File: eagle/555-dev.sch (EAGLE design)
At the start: 28 parts, among them IC1 NE555, Q1 IRF740, T1 2N2222

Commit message: change CAP
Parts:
- C2, C3, C4: device SparkFun-Passives:CAPPTH -> SparkFun-Passives:CAPPTH1
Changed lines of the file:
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@@
 <part name="R4" library="SparkFun-Resistors" deviceset="RESISTOR" device="PTH-1/4W" value="220"/>
 <part name="GND1" library="supply1" deviceset="GND" device=""/>
-<part name="C2" library="SparkFun-Passives" deviceset="CAP" device="PTH" value="0.01uF"/>
+<part name="C2" library="SparkFun-Passives" deviceset="CAP" device="PTH1" value="0.01uF"/>
 <part name="GND2" library="supply1" deviceset="GND" device=""/>
 <part name="T1" library="adafruit" deviceset="2N2222" device=""/>
@@
 <part name="GND7" library="supply1" deviceset="GND" device=""/>
 <part name="R1" library="SparkFun-Resistors" deviceset="RESISTOR" device="PTH-1/4W" value="1K"/>
-<part name="C4" library="SparkFun-Passives" deviceset="CAP" device="PTH" value="0.1uF"/>
+<part name="C4" library="SparkFun-Passives" deviceset="CAP" device="PTH1" value="0.1uF"/>
 <part name="VR" library="SparkFun-Electromechanical" deviceset="POT" device="ALPS-KIT" value="50K"/>
 <part name="GND9" library="supply1" deviceset="GND" device=""/>
@@
 <part name="P+6" library="supply1" deviceset="VCC" device=""/>
 <part name="GND8" library="supply1" deviceset="GND" device=""/>
-<part name="C3" library="SparkFun-Passives" deviceset="CAP" device="PTH" value="0.1uF"/>
+<part name="C3" library="SparkFun-Passives" deviceset="CAP" device="PTH1" value="0.1uF"/>
 <part name="GND10" library="supply1" deviceset="GND" device=""/>
 <part name="P+1" library="supply1" deviceset="VCC" device=""/>

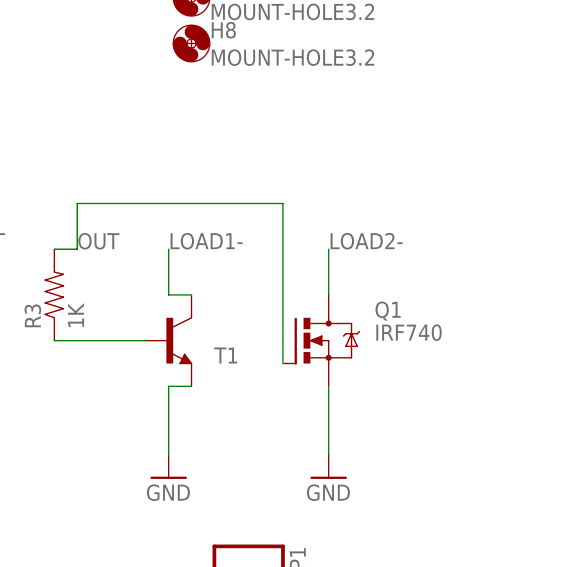
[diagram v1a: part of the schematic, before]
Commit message: add R2 base resistor and change Q1 into TIP120/IRF740
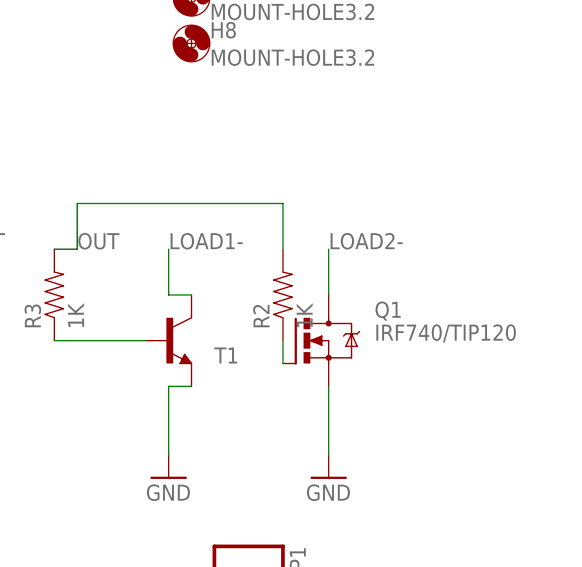
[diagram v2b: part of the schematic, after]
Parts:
- added R2: 1K, SparkFun-Resistors:RESISTORPTH-1/4W
- Q1: value IRF740 -> IRF740/TIP120
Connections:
- new net N$1: Q1.G, R2.1
- net OUT: now also R2.2; no longer Q1.G
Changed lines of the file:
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@@
 <?xml version="1.0" encoding="utf-8"?>
 <!DOCTYPE eagle SYSTEM "eagle.dtd">
-<eagle version="7.4.0">
+<eagle version="7.2.0">
 <drawing>
 <settings>
@@
 <grid distance="0.1" unitdist="inch" unit="inch" style="lines" multiple="1" display="no" altdistance="0.01" altunitdist="inch" altunit="inch"/>
 <layers>
-<layer number="1" name="Top" color="4" fill="1" visible="yes" active="no"/>
-<layer number="16" name="Bottom" color="1" fill="1" visible="yes" active="no"/>
-<layer number="17" name="Pads" color="2" fill="1" visible="yes" active="no"/>
-<layer number="18" name="Vias" color="2" fill="1" visible="yes" active="no"/>
-<layer number="19" name="Unrouted" color="6" fill="1" visible="yes" active="no"/>
-<layer number="20" name="Dimension" color="15" fill="1" visible="yes" active="no"/>
-<layer number="21" name="tPlace" color="7" fill="1" visible="yes" active="no"/>
-<layer number="22" name="bPlace" color="7" fill="1" visible="yes" active="no"/>
-<layer number="23" name="tOrigins" color="15" fill="1" visible="yes" active="no"/>
-<layer number="24" name="bOrigins" color="15" fill="1" visible="yes" active="no"/>
-<layer number="25" name="tNames" color="7" fill="1" visible="yes" active="no"/>
-<layer number="26" name="bNames" color="7" fill="1" visible="yes" active="no"/>
-<layer number="27" name="tValues" color="7" fill="1" visible="yes" active="no"/>
-<layer number="28" name="bValues" color="7" fill="1" visible="yes" active="no"/>
+<layer number="1" name="Top" color="4" fill="1" visible="no" active="no"/>
+<layer number="16" name="Bottom" color="1" fill="1" visible="no" active="no"/>
+<layer number="17" name="Pads" color="2" fill="1" visible="no" active="no"/>
+<layer number="18" name="Vias" color="2" fill="1" visible="no" active="no"/>
+<layer number="19" name="Unrouted" color="6" fill="1" visible="no" active="no"/>
+<layer number="20" name="Dimension" color="15" fill="1" visible="no" active="no"/>
+<layer number="21" name="tPlace" color="7" fill="1" visible="no" active="no"/>
+<layer number="22" name="bPlace" color="7" fill="1" visible="no" active="no"/>
+<layer number="23" name="tOrigins" color="15" fill="1" visible="no" active="no"/>
+<layer number="24" name="bOrigins" color="15" fill="1" visible="no" active="no"/>
+<layer number="25" name="tNames" color="7" fill="1" visible="no" active="no"/>
+<layer number="26" name="bNames" color="7" fill="1" visible="no" active="no"/>
+<layer number="27" name="tValues" color="7" fill="1" visible="no" active="no"/>
+<layer number="28" name="bValues" color="7" fill="1" visible="no" active="no"/>
 <layer number="29" name="tStop" color="7" fill="3" visible="no" active="no"/>
 <layer number="30" name="bStop" color="7" fill="6" visible="no" active="no"/>
@@
 <layer number="35" name="tGlue" color="7" fill="4" visible="no" active="no"/>
 <layer number="36" name="bGlue" color="7" fill="5" visible="no" active="no"/>
-<layer number="37" name="tTest" color="7" fill="1" visible="yes" active="no"/>
-<layer number="38" name="bTest" color="7" fill="1" visible="yes" active="no"/>
+<layer number="37" name="tTest" color="7" fill="1" visible="no" active="no"/>
+<layer number="38" name="bTest" color="7" fill="1" visible="no" active="no"/>
 <layer number="39" name="tKeepout" color="4" fill="11" visible="no" active="no"/>
 <layer number="40" name="bKeepout" color="1" fill="11" visible="no" active="no"/>
@@
 <layer number="44" name="Drills" color="7" fill="1" visible="no" active="no"/>
 <layer number="45" name="Holes" color="7" fill="1" visible="no" active="no"/>
-<layer number="46" name="Milling" color="3" fill="1" visible="yes" active="no"/>
-<layer number="47" name="Measures" color="7" fill="1" visible="yes" active="no"/>
-<layer number="48" name="Document" color="7" fill="1" visible="yes" active="no"/>
-<layer number="49" name="Reference" color="7" fill="1" visible="yes" active="no"/>
-<layer number="50" name="dxf" color="7" fill="1" visible="yes" active="no"/>
-<layer number="51" name="tDocu" color="7" fill="1" visible="yes" active="no"/>
-<layer number="52" name="bDocu" color="7" fill="1" visible="yes" active="no"/>
-<layer number="53" name="tGND_GNDA" color="7" fill="9" visible="yes" active="no"/>
-<layer number="54" name="bGND_GNDA" color="1" fill="9" visible="yes" active="no"/>
-<layer number="56" name="wert" color="7" fill="1" visible="yes" active="no"/>
-<layer number="57" name="tCAD" color="7" fill="1" visible="yes" active="no"/>
-<layer number="59" name="tCarbon" color="7" fill="1" visible="yes" active="no"/>
-<layer number="60" name="bCarbon" color="7" fill="1" visible="yes" active="no"/>
+<layer number="46" name="Milling" color="3" fill="1" visible="no" active="no"/>
+<layer number="47" name="Measures" color="7" fill="1" visible="no" active="no"/>
+<layer number="48" name="Document" color="7" fill="1" visible="no" active="no"/>
+<layer number="49" name="Reference" color="7" fill="1" visible="no" active="no"/>
+<layer number="50" name="dxf" color="7" fill="1" visible="no" active="no"/>
+<layer number="51" name="tDocu" color="7" fill="1" visible="no" active="no"/>
+<layer number="52" name="bDocu" color="7" fill="1" visible="no" active="no"/>
+<layer number="53" name="tGND_GNDA" color="7" fill="9" visible="no" active="no"/>
+<layer number="54" name="bGND_GNDA" color="1" fill="9" visible="no" active="no"/>
+<layer number="56" name="wert" color="7" fill="1" visible="no" active="no"/>
+<layer number="57" name="tCAD" color="7" fill="1" visible="no" active="no"/>
+<layer number="59" name="tCarbon" color="7" fill="1" visible="no" active="no"/>
+<layer number="60" name="bCarbon" color="7" fill="1" visible="no" active="no"/>
 <layer number="90" name="Modules" color="5" fill="1" visible="yes" active="yes"/>
 <layer number="91" name="Nets" color="2" fill="1" visible="yes" active="yes"/>
@@
 <part name="GND2" library="supply1" deviceset="GND" device=""/>
 <part name="T1" library="adafruit" deviceset="2N2222" device=""/>
-<part name="Q1" library="transistor-power" deviceset="IRF740" device=""/>
+<part name="Q1" library="transistor-power" deviceset="IRF740" device="" value="IRF740/TIP120"/>
 <part name="GND4" library="supply1" deviceset="GND" device=""/>
 <part name="GND6" library="supply1" deviceset="GND" device=""/>
@@
 <part name="GND3" library="supply1" deviceset="GND" device=""/>
 <part name="U$1" library="SparkFun-Electromechanical" deviceset="LOGO" device=""/>
+<part name="R2" library="SparkFun-Resistors" deviceset="RESISTOR" device="PTH-1/4W" value="1K"/>
 </parts>
 <sheets>
@@
 <instance part="GND3" gate="1" x="111.76" y="76.2"/>
 <instance part="U$1" gate="G$1" x="33.02" y="86.36"/>
+<instance part="R2" gate="G$1" x="160.02" y="35.56" rot="R90"/>
 </instances>
 <busses>
@@
 <label x="137.16" y="40.64" size="1.778" layer="95"/>
 <wire x1="137.16" y1="40.64" x2="137.16" y2="45.72" width="0.1524" layer="91"/>
-<pinref part="Q1" gate="G$1" pin="G"/>
 <wire x1="137.16" y1="45.72" x2="160.02" y2="45.72" width="0.1524" layer="91"/>
-<wire x1="160.02" y1="45.72" x2="160.02" y2="27.94" width="0.1524" layer="91"/>
+<pinref part="R2" gate="G$1" pin="2"/>
+<wire x1="160.02" y1="40.64" x2="160.02" y2="45.72" width="0.1524" layer="91"/>
 </segment>
 </net>
@@
 </segment>
 </net>
+<net name="N$1" class="0">
+<segment>
+<pinref part="Q1" gate="G$1" pin="G"/>
+<pinref part="R2" gate="G$1" pin="1"/>
+<wire x1="160.02" y1="30.48" x2="160.02" y2="27.94" width="0.1524" layer="91"/>
+</segment>
+</net>

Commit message: added base R
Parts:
- removed PR1, PR2: PHOTOCELLPTH-KIT, SparkFun-Sensors:PHOTOCELLPTH-KIT
- added R5, R6: (no value), Discrete:R-PHOTOVARISTOR'0546'
- JP1, JP2: device SparkFun-Connectors:M023.5MM-NO_SILK -> SparkFun-Connectors:M022.54MM_SCREWTERM
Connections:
- net LOAD1-: now also JP1.1; no longer JP1.2
- net LOAD2-: now also JP2.1; no longer JP2.2
- net N$2: now also R6.P$1; no longer PR2.P$1
- net N$3: now also R5.P$1; no longer PR1.P$1
- net PR1: now also R5.P$2; no longer PR1.P$2
- net PR2: now also R6.P$2; no longer PR2.P$2
- net VCC: now also JP1.2, JP2.2; no longer JP1.1, JP2.1
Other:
- moved on the sheet: D1, D4, JP1, JP2
